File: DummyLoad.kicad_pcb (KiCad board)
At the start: 2 copper layers, 71 x 37 mm, 37 parts, among them J1 RF In, J2 RF Out

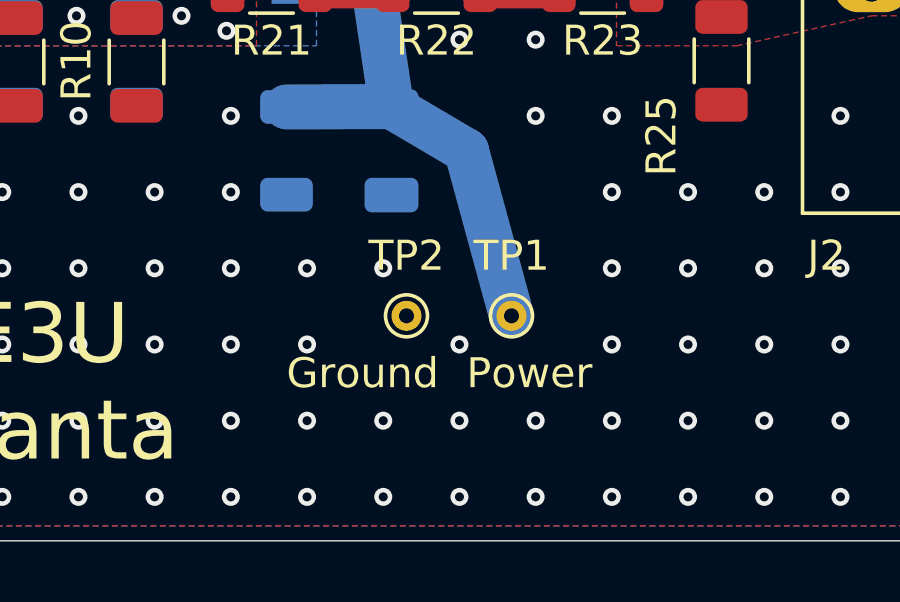
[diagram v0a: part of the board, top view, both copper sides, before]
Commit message: Enlarge THT test points and update PCB layout
Replace TP1/TP2 footprints with larger THT test points (TestPoint_THTPad_D3.0mm_Drill1.5mm): pad sizes and drill diameters increased from 1.0/0.5mm to 3.0/1.5mm, and related silk/fab text positions and silk radii adjusted. Many via coordinates and UUIDs were updated/refreshed, and a few silkscreen text anchors ("Power", "Ground") were nudged. DummyLoad.kicad_sch was also modified alongside these PCB changes. Reason: accommodate larger test probes and tidy up PCB placement/identifiers.
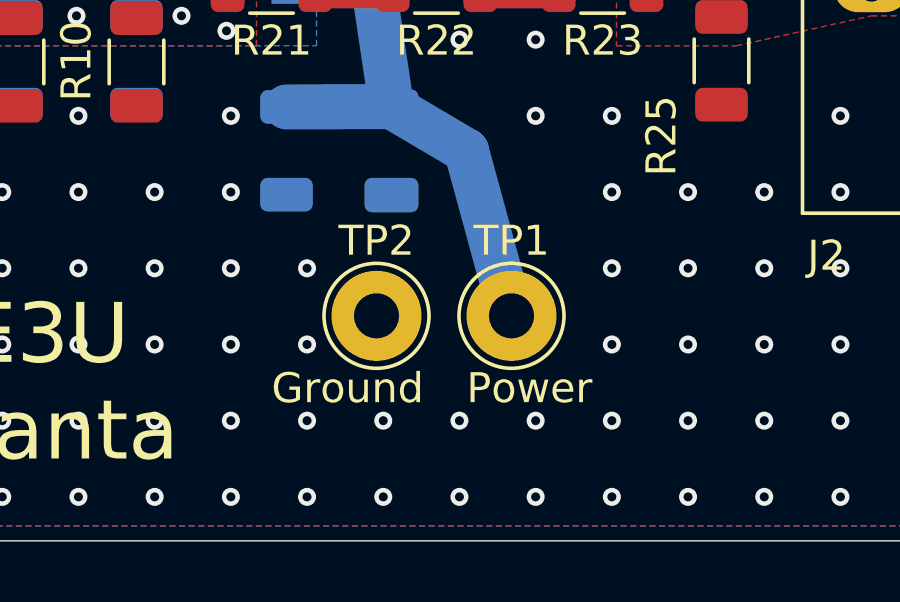
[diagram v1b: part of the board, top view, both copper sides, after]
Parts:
- TP1, TP2: footprint TestPoint:TestPoint_THTPad_D1.0mm_Drill0.5mm -> TestPoint:TestPoint_THTPad_D3.0mm_Drill1.5mm
- moved TP2 1.00 mm to (140.5, 87.0)
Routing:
- net GND: vias 272 -> 270

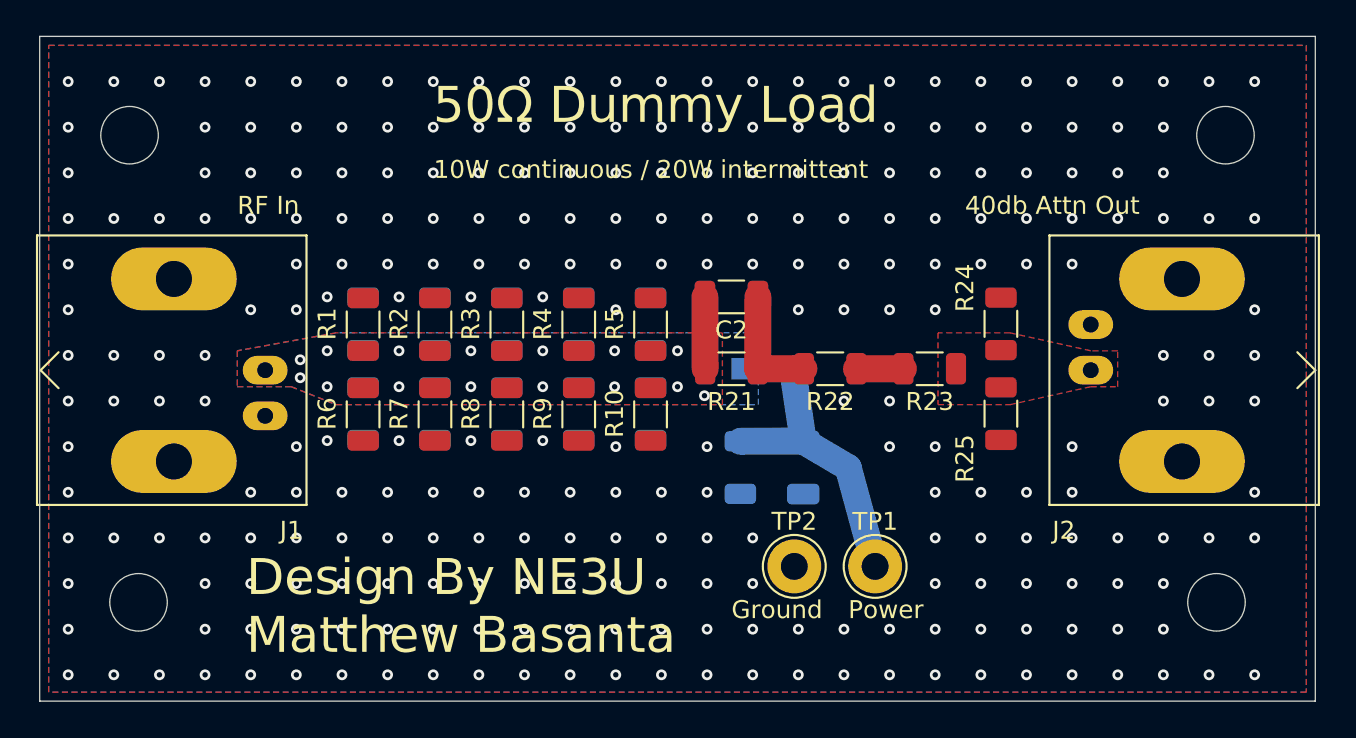
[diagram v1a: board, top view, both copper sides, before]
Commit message: Use hand-solder 1206 resistor footprints
Replace Resistor_SMD:R_1206_3216Metric with R_1206_3216Metric_Pad1.30x1.75mm_HandSolder across the PCB. Pads enlarged from 1.125x1.75 to 1.30x1.75 (adjusted roundrect ratio) and pad positions/rotations slightly tweaked; courtyard/silkscreen lines and text orientations updated. UUIDs and metadata/tags/descriptions updated, and zone_connect attributes removed where present. These changes provide elongated pads for easier hand-soldering and consistent footprint metadata.
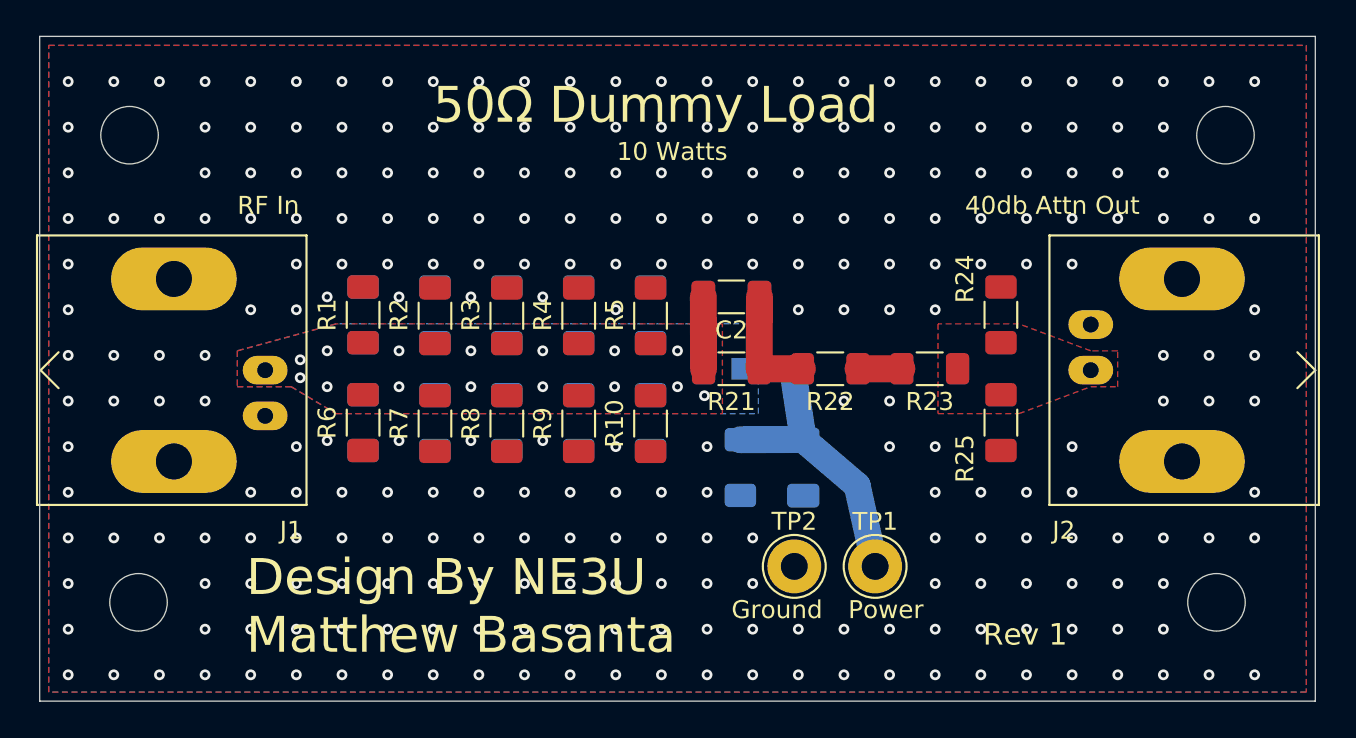
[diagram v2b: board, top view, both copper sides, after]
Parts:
- C1, C2: footprint Capacitor_SMD:C_1206_3216Metric -> Capacitor_SMD:C_1206_3216Metric_Pad1.33x1.80mm_HandSolder
- R1, R10, R11, R12, R13, R14, R15, R16, R17, R18, R19, R2, R20, R21, R22, R23, R24, R25, R26, R3, R4, R5, R6, R7, R8, R9: footprint Resistor_SMD:R_1206_3216Metric -> Resistor_SMD:R_1206_3216Metric_Pad1.30x1.75mm_HandSolder
- moved R1 0.54 mm to (116.5, 73.0)
- moved R10 0.51 mm to (132.5, 79.0)
- moved R7 0.51 mm to (120.5, 79.0)
- moved R8 0.51 mm to (124.5, 79.0)
- moved R9 0.51 mm to (128.5, 79.0)
- moved R11 0.50 mm to (132.5, 73.0)
- moved R12 0.50 mm to (128.5, 73.0)
- moved R13 0.50 mm to (124.5, 73.0)
- moved R14 0.50 mm to (120.5, 73.0)
- moved R15 0.50 mm to (116.5, 73.0)
- moved R16 0.50 mm to (132.5, 79.0)
- moved R17 0.50 mm to (128.5, 79.0)
- moved R18 0.50 mm to (124.5, 79.0)
- moved R19 0.50 mm to (120.5, 79.0)
- moved R20 0.50 mm to (116.5, 79.0)
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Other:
- board text added: "10 Watts"
- board text added: "Rev 1"
- board text removed: "10W continuous / 20W intermittent"
